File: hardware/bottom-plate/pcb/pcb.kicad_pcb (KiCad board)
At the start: 4 copper layers, 218 x 205.9 mm, 254 parts, among them SW1 MT-0-102-A101-M200-RS+PJ, SW2 TS4535TP 250GF 009, SW3 TS4535TP 250GF 009

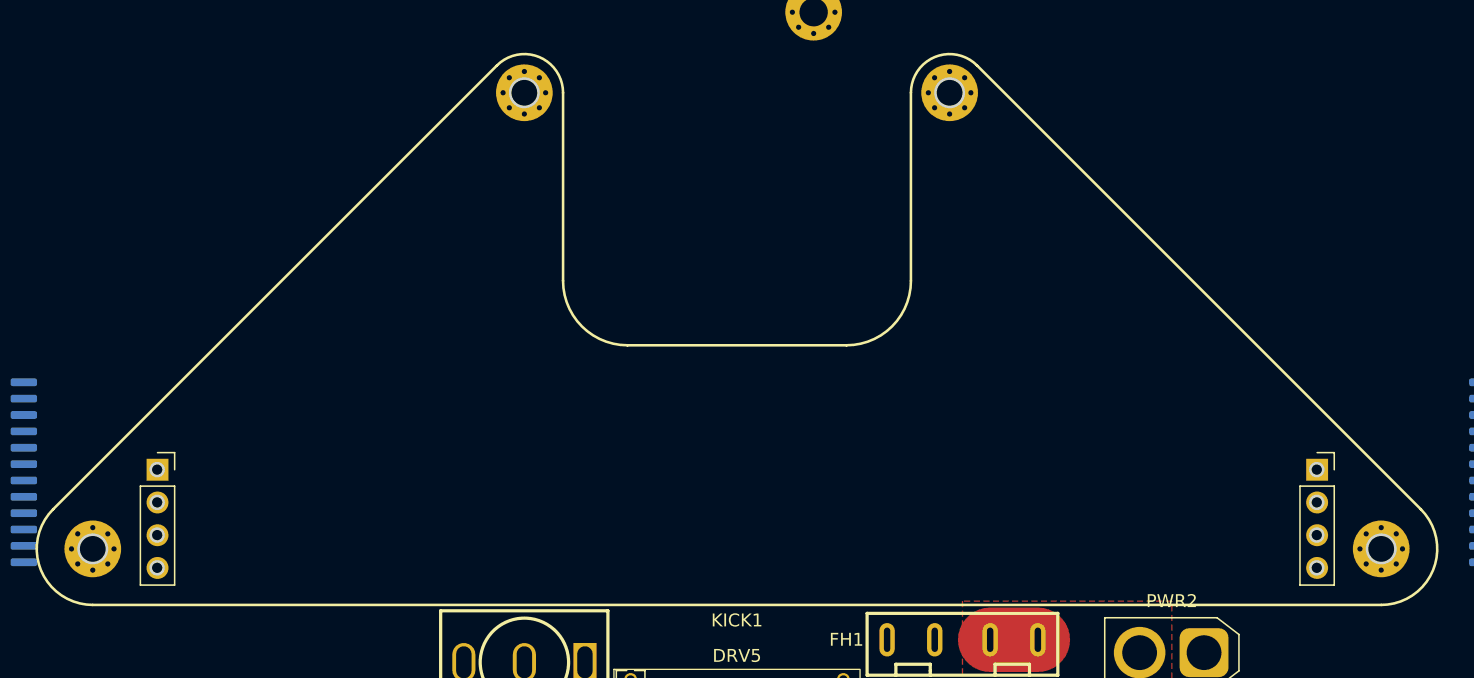
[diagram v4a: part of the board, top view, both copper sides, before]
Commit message: made copper zone connections solid
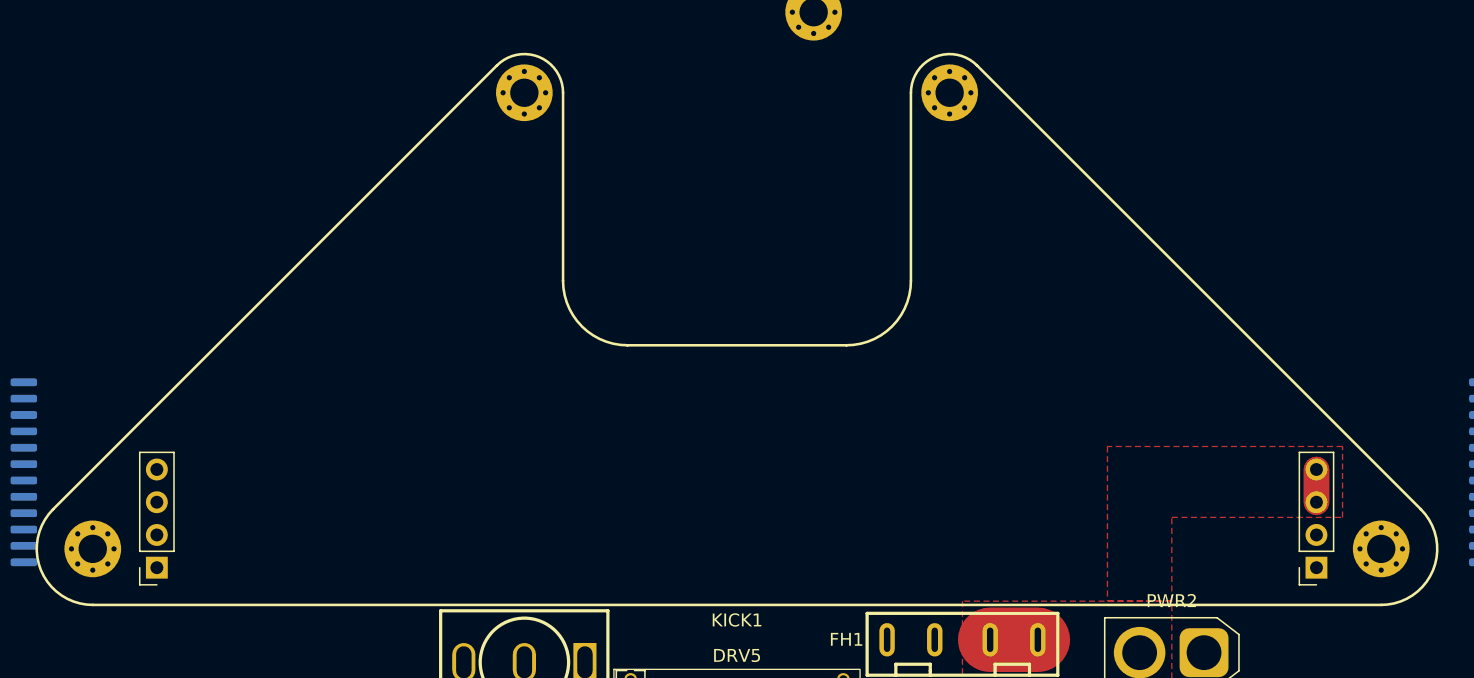
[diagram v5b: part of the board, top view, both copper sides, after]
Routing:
- net VCC: track 22.2 -> 24.7 mm
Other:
- outline, holes or cut-outs redrawn

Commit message: fixed line sensor positions
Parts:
- removed FH1: XF-506P, EasyEDA:FUSE-TH_XF-506P
- ADC1, ADC2, DMUX1, DMUX2: moved to B.Cu
- H1, H2, H3, H4, H5, H6, H7, H8: footprint MountingHole:MountingHole_2.2mm_M2_Pad_Via -> MountingHole:MountingHole_3.2mm_M3_Pad_Via
- moved ADC2 215.1 mm to (-22.5, -60.0), turned to 180 degrees
- moved JP8 191.9 mm to (-21.2, -63.5), turned to -90 degrees
- moved R2 182.8 mm to (12.0, 56.5), turned to -90 degrees
- moved R1 180.0 mm to (14.5, 56.5), turned to -90 degrees
- moved ADC1 172.2 mm to (22.5, -60.0), turned to 180 degrees
- moved JP7 161.8 mm to (21.2, -63.5), turned to 90 degrees
- moved GATE_LED1 132.8 mm to (-20.5, -51.2), turned to 90 degrees
- moved DMUX2 131.7 mm to (82.0, 94.0), turned to 180 degrees
- moved LOADCELL1 112.8 mm to (-29.5, -64.0), turned to -90 degrees
- moved LIGHTGATE1 77.2 mm to (29.5, -57.5), turned to 90 degrees
- moved AMUX1 2.75 mm to (65.2, 0.00), turned to 180 degrees
- turned DMUX1 to 180 degrees
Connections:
- ADC1 pad 4: /DRV1_IPROPI -> /DRV2_IPROPI
- ADC1 pad 5: /DRV2_IPROPI -> /GATE
- ADC1 pad 6: /DRV3_IPROPI -> /DRV5_IPROPI
- ADC1 pad 7: /GATE -> /DRV3_IPROPI
- ADC2 pad 4: /DRV4_IPROPI -> /LOADCELL_A-
- ADC2 pad 5: /DRV5_IPROPI -> /LOADCELL_A+
- ADC2 pad 6: /LOADCELL_A+ -> /DRV1_IPROPI
- ADC2 pad 7: /LOADCELL_A- -> /DRV4_IPROPI
- AMUX1 pad 2: /line sensor array 1/LS8 -> /line sensor array 1/LS1
- AMUX1 pad 3: /line sensor array 1/LS7 -> /line sensor array 1/LS2
- AMUX1 pad 4: /line sensor array 1/LS6 -> /line sensor array 1/LS3
- AMUX1 pad 5: /line sensor array 1/LS5 -> /line sensor array 1/LS4
- AMUX1 pad 6: /line sensor array 1/LS4 -> /line sensor array 1/LS5
- AMUX1 pad 7: /line sensor array 1/LS3 -> /line sensor array 1/LS6
- AMUX1 pad 8: /line sensor array 1/LS2 -> /line sensor array 1/LS7
- AMUX1 pad 9: /line sensor array 1/LS1 -> /line sensor array 1/LS8
- AMUX2 pad 2: /line sensor array 2/LS8 -> /line sensor array 2/LS1
- AMUX2 pad 3: /line sensor array 2/LS7 -> /line sensor array 2/LS2
- AMUX2 pad 4: /line sensor array 2/LS6 -> /line sensor array 2/LS3
- AMUX2 pad 5: /line sensor array 2/LS5 -> /line sensor array 2/LS4
- AMUX2 pad 6: /line sensor array 2/LS4 -> /line sensor array 2/LS5
- AMUX2 pad 7: /line sensor array 2/LS3 -> /line sensor array 2/LS6
- AMUX2 pad 8: /line sensor array 2/LS2 -> /line sensor array 2/LS7
- AMUX2 pad 9: /line sensor array 2/LS1 -> /line sensor array 2/LS8
- AMUX3 pad 2: /line sensor array 3/LS8 -> /line sensor array 3/LS1
- AMUX3 pad 3: /line sensor array 3/LS7 -> /line sensor array 3/LS2
- AMUX3 pad 4: /line sensor array 3/LS6 -> /line sensor array 3/LS3
- AMUX3 pad 5: /line sensor array 3/LS5 -> /line sensor array 3/LS4
- AMUX3 pad 6: /line sensor array 3/LS4 -> /line sensor array 3/LS5
- AMUX3 pad 7: /line sensor array 3/LS3 -> /line sensor array 3/LS6
- AMUX3 pad 8: /line sensor array 3/LS2 -> /line sensor array 3/LS7
- AMUX3 pad 9: /line sensor array 3/LS1 -> /line sensor array 3/LS8
- DRV1 pad 10: /DRV5_IPROPI -> /DRV1_IPROPI
- DRV1 pad 11: /DRV5_NSLEEP -> /DRV1_NSLEEP
- DRV1 pad 2: /DRV5_SCS -> /DRV1_SCS
- DRV1 pad 3: /DRV5_IN2 -> /DRV1_IN2
- DRV1 pad 4: /DRV5_IN1 -> /DRV1_IN1
- DRV1 pad 5: /DRV5_OFF -> /DRV1_OFF
- DRV1 pad 9: /DRV5_NFAULT -> /DRV1_NFAULT
- DRV2 pad 10: /DRV4_IPROPI -> /DRV2_IPROPI
- DRV2 pad 11: /DRV4_NSLEEP -> /DRV2_NSLEEP
- DRV2 pad 2: /DRV4_SCS -> /DRV2_SCS
- DRV2 pad 3: /DRV4_IN2 -> /DRV2_IN2
- DRV2 pad 4: /DRV4_IN1 -> /DRV2_IN1
- DRV2 pad 5: /DRV4_OFF -> /DRV2_OFF
- DRV2 pad 9: /DRV4_NFAULT -> /DRV2_NFAULT
- DRV4 pad 10: /DRV2_IPROPI -> /DRV4_IPROPI
- DRV4 pad 11: /DRV2_NSLEEP -> /DRV4_NSLEEP
- DRV4 pad 2: /DRV2_SCS -> /DRV4_SCS
- DRV4 pad 3: /DRV2_IN2 -> /DRV4_IN2
- DRV4 pad 4: /DRV2_IN1 -> /DRV4_IN1
- DRV4 pad 5: /DRV2_OFF -> /DRV4_OFF
- DRV4 pad 9: /DRV2_NFAULT -> /DRV4_NFAULT
- DRV5 pad 10: /DRV1_IPROPI -> /DRV5_IPROPI
- DRV5 pad 11: /DRV1_NSLEEP -> /DRV5_NSLEEP
- DRV5 pad 2: /DRV1_SCS -> /DRV5_SCS
- DRV5 pad 3: /DRV1_IN2 -> /DRV5_IN2
- DRV5 pad 4: /DRV1_IN1 -> /DRV5_IN1
- DRV5 pad 5: /DRV1_OFF -> /DRV5_OFF
- DRV5 pad 9: /DRV1_NFAULT -> /DRV5_NFAULT
- GATE_LED1 pad 1: +5V -> GND
- GATE_LED1 pad 2: GND -> +5V
- LIGHTGATE1 pad 1: /GATE -> GND
- LIGHTGATE1 pad 2: GND -> /GATE
- LOADCELL1 pad 1: +3V3 -> GND
- LOADCELL1 pad 2: /LOADCELL_A+ -> /LOADCELL_A-
- LOADCELL1 pad 3: /LOADCELL_A- -> /LOADCELL_A+
- LOADCELL1 pad 4: GND -> +3V3
- PWR1 pad 2: VCC_NFUSE -> VCC
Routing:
- net +3V3: track 0.00 -> 1011.1 mm, vias 0 -> 78
- net +5V: track 0.00 -> 181.7 mm, vias 0 -> 48
- net VCC: track 24.7 -> 0.00 mm
- net /LOADCELL_A-: track 0.00 -> 10.7 mm
- net /LOADCELL_A+: track 0.00 -> 9.83 mm
- net GND: track 128.2 -> 134.4 mm, vias 96 -> 100
- net Net-(ADC2-ADDR): track 0.00 -> 3.39 mm
- net Net-(ADC1-ADDR): track 0.00 -> 3.39 mm
- net /line sensor array 3/LS4: track 2.26 -> 5.19 mm, vias 0 -> 2
- net /line sensor array 3/LS1: track 2.26 -> 5.18 mm, vias 0 -> 2
- net /line sensor array 3/LS8: track 2.26 -> 5.18 mm, vias 0 -> 2
- net /line sensor array 3/LS5: track 2.26 -> 5.17 mm, vias 0 -> 2
- net /line sensor array 3/LS13: track 2.26 -> 5.17 mm, vias 0 -> 2
- net /line sensor array 3/LS2: track 2.26 -> 5.17 mm, vias 0 -> 2
- net /line sensor array 3/LS10: track 2.26 -> 5.16 mm, vias 0 -> 2
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- added copper zone on F.Cu, net +3V3
- added copper zone on F.Cu, net +5V
- added copper zone on F.Cu, net Net-(BUCK1-IN+)
